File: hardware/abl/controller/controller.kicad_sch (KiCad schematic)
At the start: 38 parts, among them IC2 FXL6408UMX, IC3 VEML6040A3OG, IC4 FXL6408UMX, J1 SFW20S-2STE1LF, J2 Conn_02x05_Odd_Even, J3 Conn_02x05_Odd_Even, J4 PRT-14417, J5 Conn_02x05_Odd_Even, Q2 AO3401A, Q4 AO3401A, U1 INA219AxD, U2 TXB0104RUT

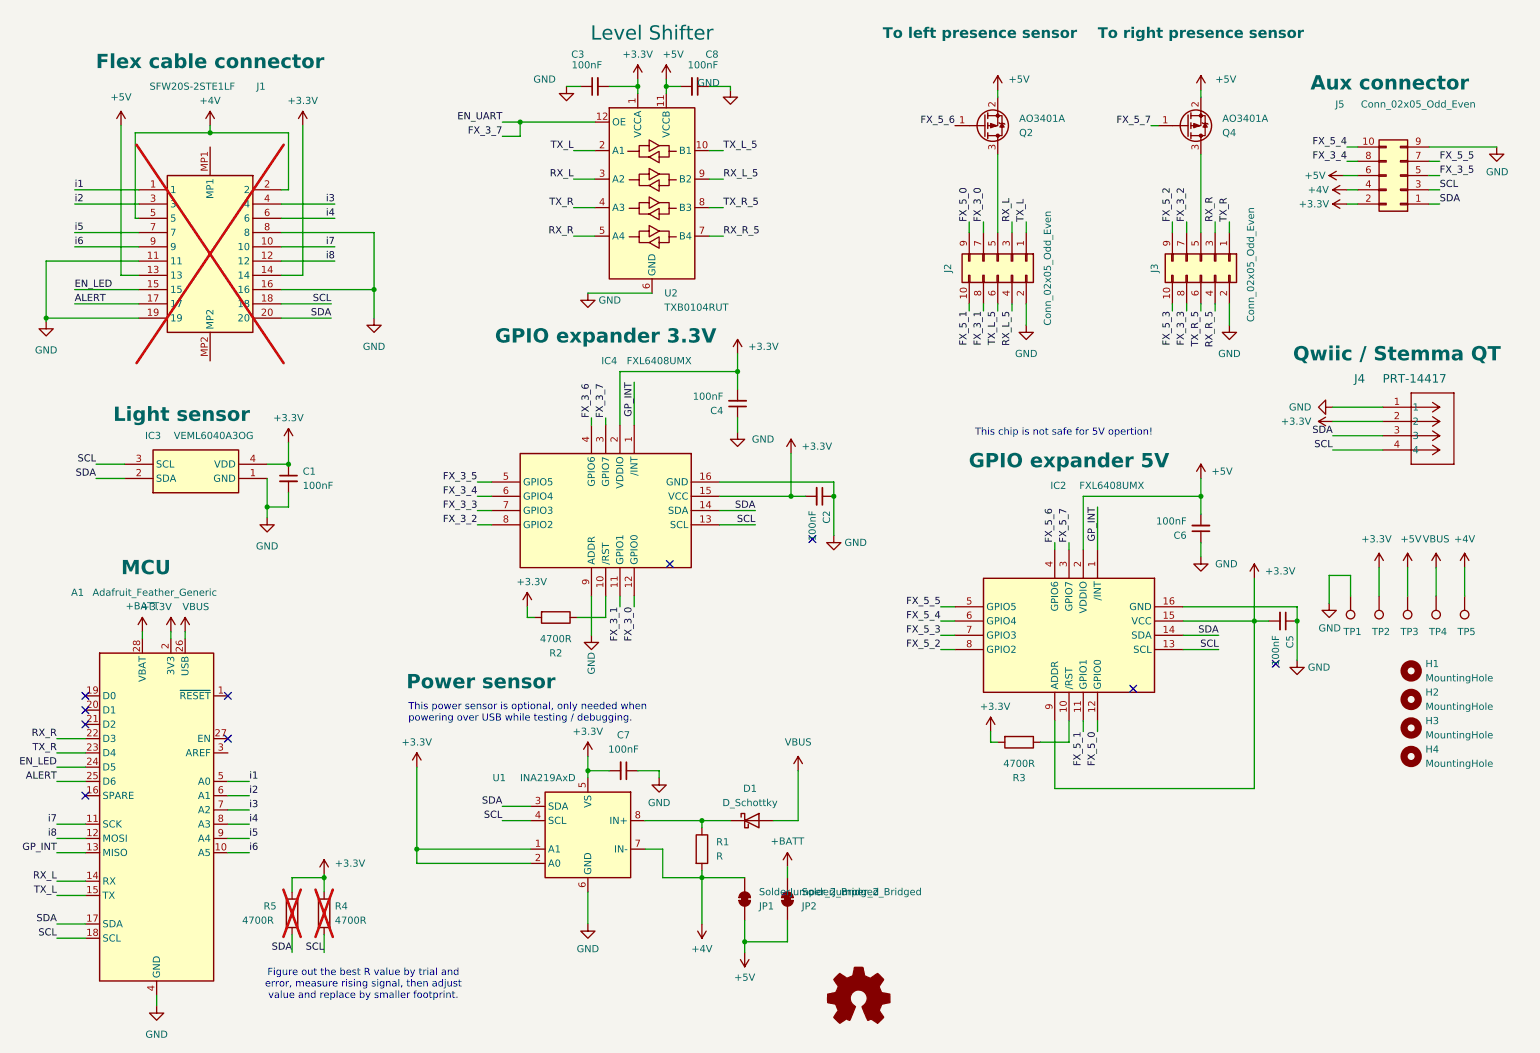
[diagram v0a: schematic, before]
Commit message: Exchanged GPIO Expander for one that supports 5V.
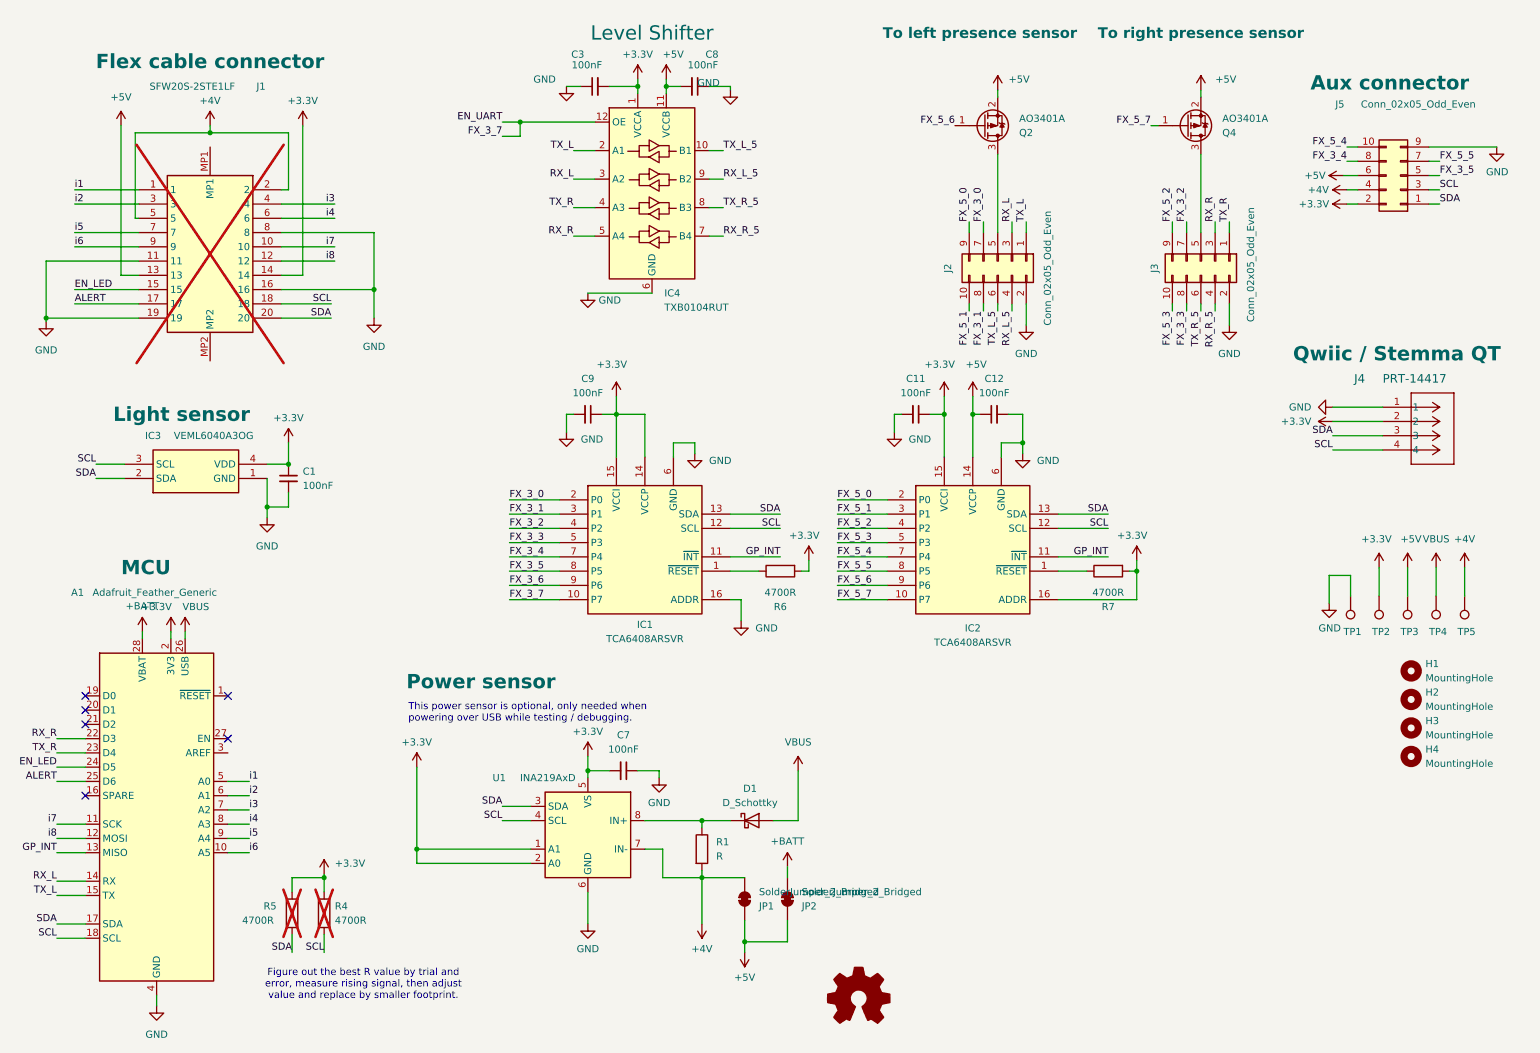
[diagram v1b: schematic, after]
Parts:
- removed C2, C4, C5, C6: 100nF, Capacitor_SMD:C_0402_1005Metric, symbol Device:C_Small
- removed IC2, IC4: FXL6408UMX, QFN40P180X260X55-16N, symbol FXL6408UMX:FXL6408UMX
- removed R2, R3: 4700R, Resistor_SMD:R_0402_1005Metric, symbol Device:R
- added C11, C12, C9: 100nF, Capacitor_SMD:C_0402_1005Metric, symbol Device:C_Small
- added IC1, IC2: TCA6408ARSVR, QFN40P180X260X55-16N, symbol TCA6408ARSVR:TCA6408ARSVR_Own
- added R6, R7: 4700R, Resistor_SMD:R_0402_1005Metric, symbol Device:R
- renumbered U2 to IC4
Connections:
- net +3.3V: now also C11.1, C9.1, IC1.14 (VCCP), IC1.15 (VCCI), IC2.15 (VCCI), IC2.16 (ADDR), R6.2, R7.2
- net +5V: now also C12.1, IC2.14 (VCCP)
- net EN_UART: now also IC1.10 (P7)
- net FX_3_0: now also IC1.2 (P0)
- net FX_3_1: now also IC1.3 (P1)
- net FX_3_2: now also IC1.4 (P2)
- net FX_3_3: now also IC1.5 (P3)
- net FX_3_4: now also IC1.7 (P4)
- net FX_3_5: now also IC1.8 (P5)
- net FX_3_6: now also IC1.9 (P6)
- net FX_5_0: now also IC2.2 (P0)
- net FX_5_1: now also IC2.3 (P1)
- net FX_5_2: now also IC2.4 (P2)
- net FX_5_3: now also IC2.5 (P3)
- net FX_5_4: now also IC2.7 (P4)
- net FX_5_5: now also IC2.8 (P5)
- net FX_5_6: now also IC2.9 (P6)
- net FX_5_7: now also IC2.10 (P7)
- net GND: now also C11.2, C12.2, C9.2, IC1.16 (ADDR), IC1.6 (GND), IC2.6 (GND)
- net GP_INT: now also IC1.11 (~{INT}), IC2.11 (~{INT})
- net SCL: now also IC1.12 (SCL), IC2.12 (SCL)
- net SDA: now also IC1.13 (SDA), IC2.13 (SDA)
- new net: IC1.1 (~{RESET}), R6.1
- new net: IC2.1 (~{RESET}), R7.1
- no-connect marks 10 -> 6

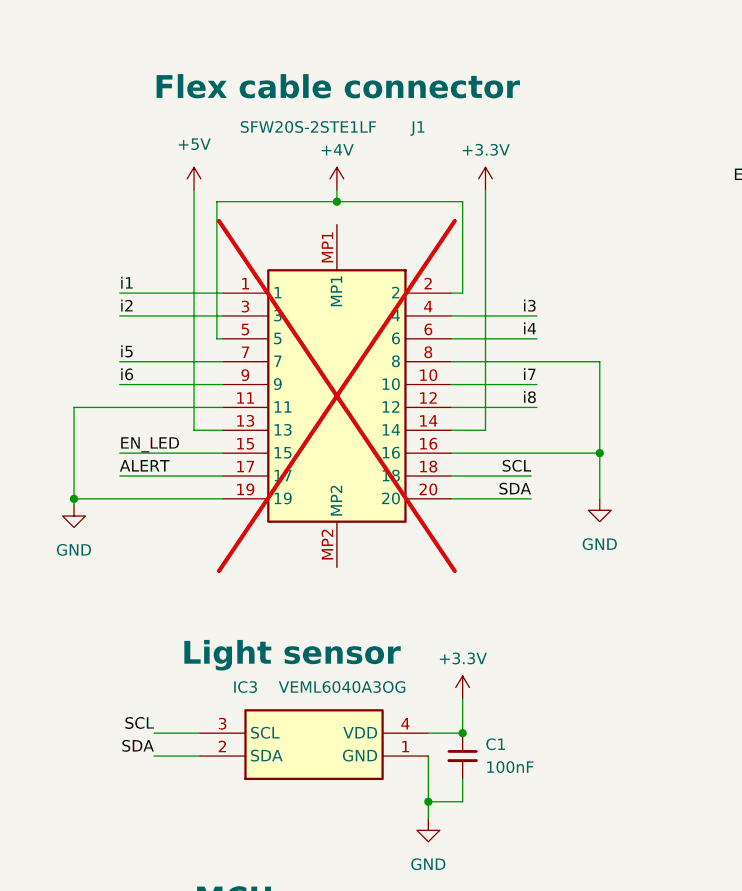
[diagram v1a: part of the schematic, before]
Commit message: Fix orientation of the flex connector.
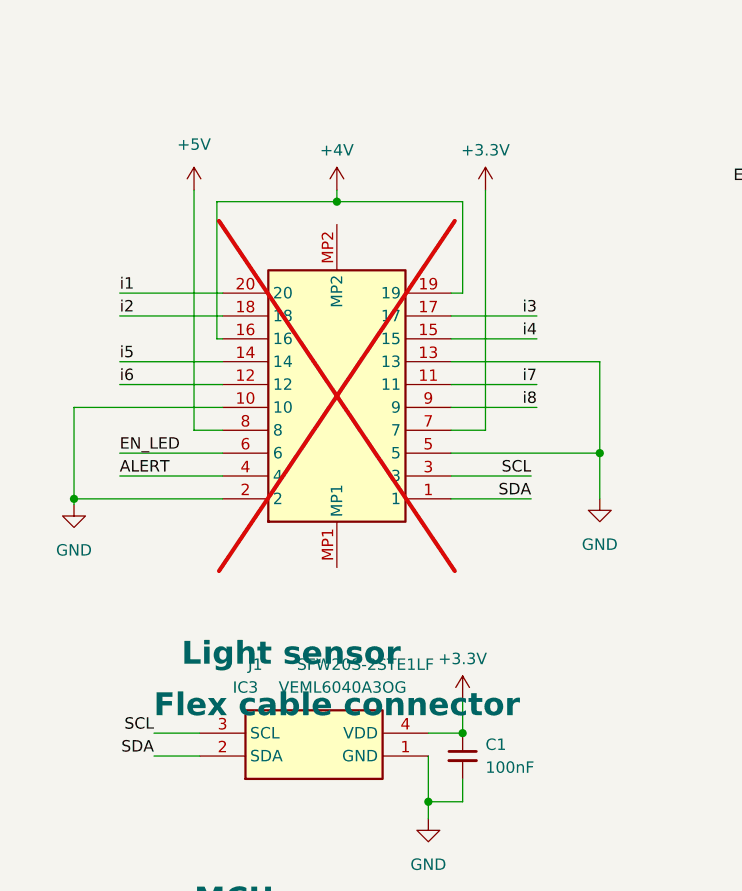
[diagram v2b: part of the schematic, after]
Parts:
- J1: footprint SFW20S2STE1LF -> Own footprints:SFW20S2STE1LF_Own
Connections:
- net +3.3V: now also J1.7; no longer J1.14
- net +4V: now also J1.16, J1.19; no longer J1.2, J1.5
- net +5V: now also J1.8; no longer J1.13
- net ALERT: now also J1.4; no longer J1.17
- net EN_LED: now also J1.6; no longer J1.15
- net GND: now also J1.10, J1.13, J1.2, J1.5; no longer J1.11, J1.16, J1.19, J1.8
- net SCL: now also J1.3; no longer J1.18
- net SDA: now also J1.1; no longer J1.20
- net i1: now also J1.20; no longer J1.1
- net i2: now also J1.18; no longer J1.3
- net i3: now also J1.17; no longer J1.4
- net i4: now also J1.15; no longer J1.6
- net i5: now also J1.14; no longer J1.7
- net i6: now also J1.12; no longer J1.9
- net i7: now also J1.11; no longer J1.10
- net i8: now also J1.9; no longer J1.12
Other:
- moved on the sheet: J1
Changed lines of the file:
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@@
 	(symbol
 		(lib_id "SFW20S-2STE1LF:SFW20S-2STE1LF")
-		(at 50.8 37.465 270)
+		(at 50.8 75.565 90)
 		(unit 1)
 		(exclude_from_sim no)
@@
 		(dnp yes)
 		(property "Reference" "J1"
-			(at 59.055 26.67 90)
+			(at 42.545 86.36 90)
 			(effects
 				(font
@@
 		)
 		(property "Value" "SFW20S-2STE1LF"
-			(at 40.005 26.67 90)
+			(at 61.595 86.36 90)
 			(effects
 				(font
@@
 			)
 		)
-		(property "Footprint" "SFW20S2STE1LF"
-			(at -39.04 71.755 0)
+		(property "Footprint" "Own footprints:SFW20S2STE1LF_Own"
+			(at 140.64 41.275 0)
 			(effects
 				(font
@@
 		)
 		(property "Datasheet" "https://cdn.amphenol-cs.com/media/wysiwyg/files/drawing/10172832.pdf"
-			(at -139.04 71.755 0)
+			(at 240.64 41.275 0)
 			(effects
 				(font
@@
 		)
 		(property "Description" "1.00mm Flex Connector, SFW Straight series, 20 Position, Top Entry Surface Mount, ZIF"
-			(at 50.8 37.465 0)
+			(at 50.8 75.565 0)
 			(effects
 				(font
@@
 		)
 		(property "Height" "5.5"
-			(at -339.04 71.755 0)
+			(at 440.64 41.275 0)
 			(effects
 				(font
@@
 		)
 		(property "Mouser Part Number" ""
-			(at -439.04 71.755 0)
+			(at 540.64 41.275 0)
 			(effects
 				(font
@@
 		)
 		(property "Mouser Price/Stock" ""
-			(at -539.04 71.755 0)
+			(at 640.64 41.275 0)
 			(effects
 				(font
@@
 		)
 		(property "Manufacturer_Name" "Amphenol Communications Solutions"
-			(at -639.04 71.755 0)
+			(at 740.64 41.275 0)
 			(effects
 				(font
@@
 		)
 		(property "Manufacturer_Part_Number" "SFW20S-2STE1LF"
-			(at -739.04 71.755 0)
+			(at 840.64 41.275 0)
 			(effects
 				(font
@@
 		)
 		(property "LCSC Part #" "C5407823"
-			(at 50.8 37.465 0)
+			(at 50.8 75.565 0)
 			(effects
 				(font
@@
 		)
 		(property "Purpose" "Flex cable connector"
-			(at 50.8 22.225 90)
+			(at 50.8 90.805 90)
 			(effects
 				(font

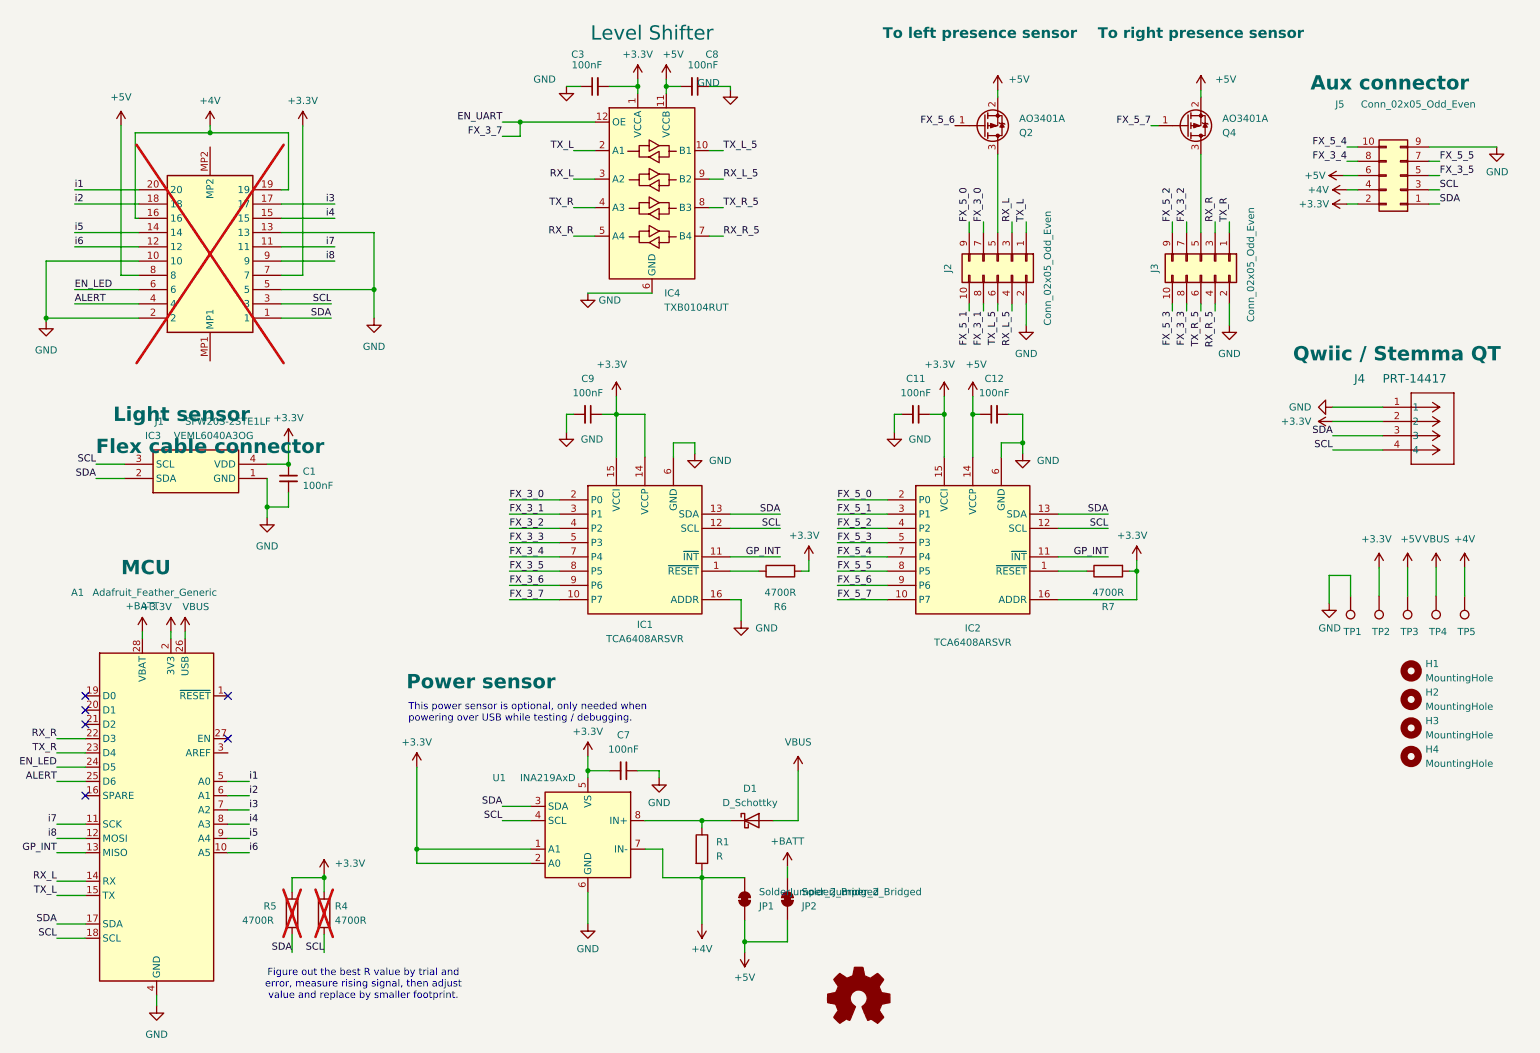
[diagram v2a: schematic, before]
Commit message: Extended with wings to attach presence sensors directly. Removed distinction between VLED and 5V. Much cleanup.
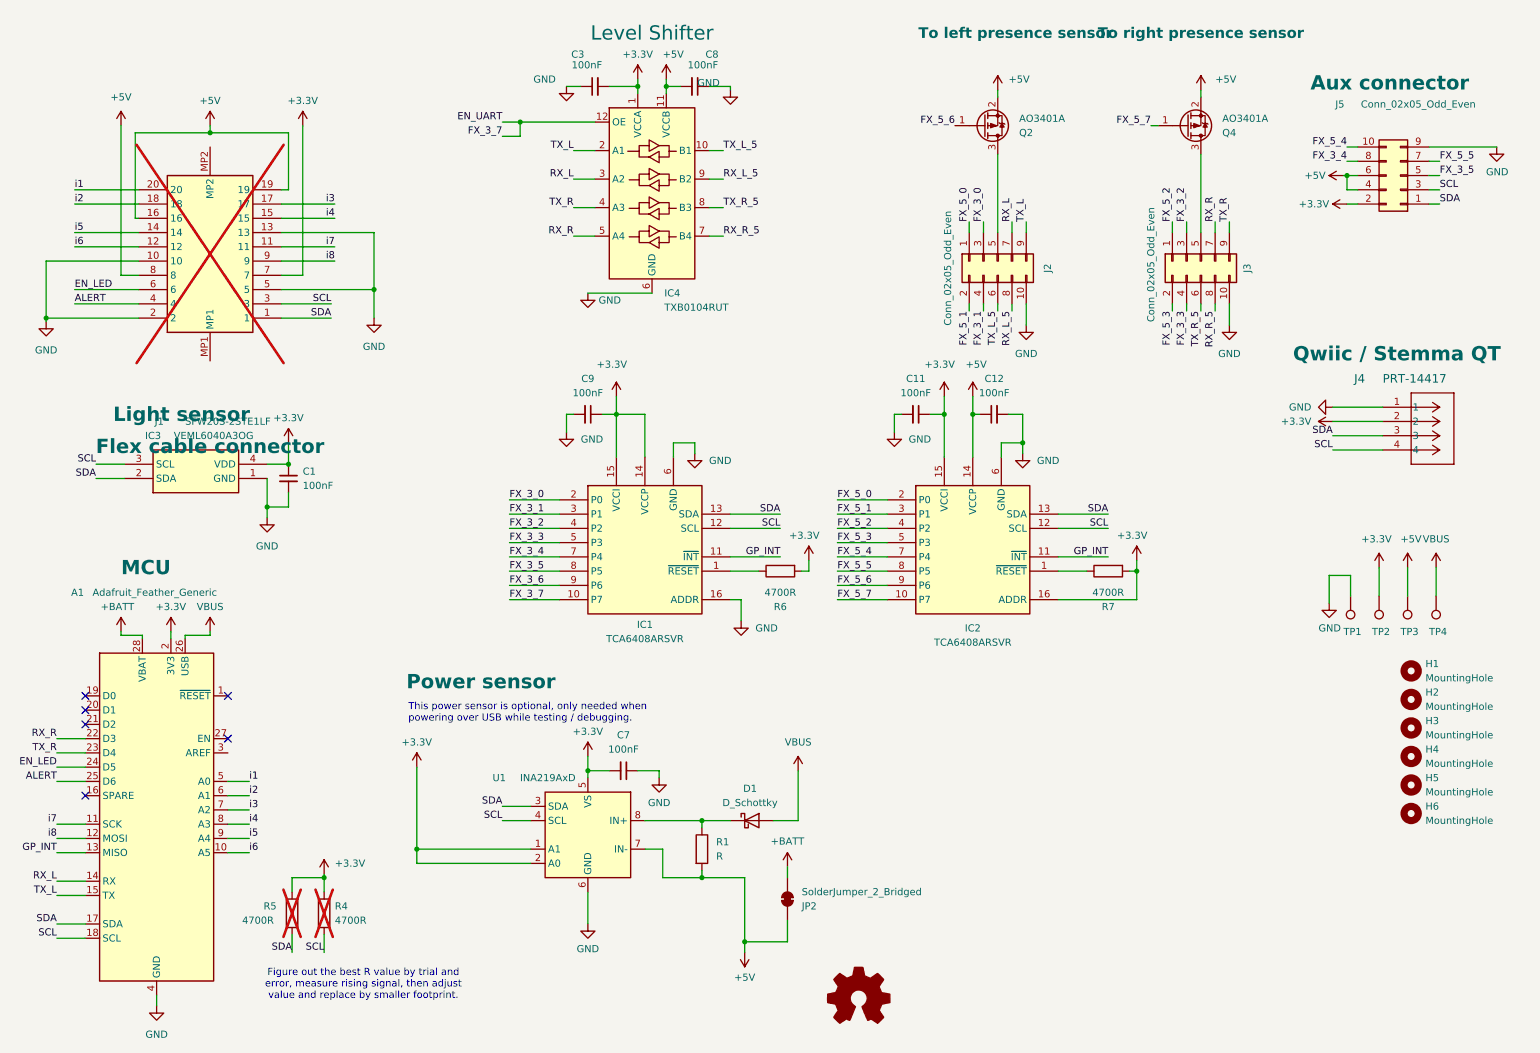
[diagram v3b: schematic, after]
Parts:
- removed JP1: SolderJumper_2_Bridged, Jumper:SolderJumper-2_P1.3mm_Bridged2Bar_RoundedPad1.0x1.5mm, symbol Jumper:SolderJumper_2_Bridged
- removed TP5: TestPoint, TestPoint:TestPoint_THTPad_D1.5mm_Drill0.7mm, symbol Connector:TestPoint
- added H5, H6: MountingHole, MountingHole:MountingHole_3.2mm_M3_DIN965, symbol Mechanical:MountingHole
- J2, J3: footprint Connector_IDC:IDC-Header_2x05_P2.54mm_Vertical -> Own footprints:Dual Row Inverted Thru Board Card Edge Connector 02x05 Kyocera AVX 009159010603906
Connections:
- net  FX_5_1 is gone; now on net GND: J2.10 (Pin_10)
- net +4V is gone; now on net +5V: J1.16, J1.19, J5.4 (Pin_4), R1.2, U1.7 (IN-)
- net FX_3_0: now also J2.3 (Pin_3); no longer J2.7 (Pin_7)
- net FX_3_1: now also J2.4 (Pin_4); no longer J2.8 (Pin_8)
- net FX_3_2: now also J3.3 (Pin_3); no longer J3.7 (Pin_7)
- net FX_3_3: now also J3.4 (Pin_4); no longer J3.8 (Pin_8)
- net FX_5_0: now also J2.1 (Pin_1); no longer J2.9 (Pin_9)
- net FX_5_1: now also J2.2 (Pin_2)
- net FX_5_2: now also J3.1 (Pin_1); no longer J3.9 (Pin_9)
- net FX_5_3: now also J3.2 (Pin_2); no longer J3.10 (Pin_10)
- net GND: now also J3.10 (Pin_10); no longer J2.2 (Pin_2), J3.2 (Pin_2)
- net RX_L: now also J2.7 (Pin_7); no longer J2.3 (Pin_3)
- net RX_L_5: now also J2.8 (Pin_8); no longer J2.4 (Pin_4)
- net RX_R: now also J3.7 (Pin_7); no longer J3.3 (Pin_3)
- net RX_R_5: now also J3.8 (Pin_8); no longer J3.4 (Pin_4)
- net TX_L: now also J2.9 (Pin_9); no longer J2.1 (Pin_1)
- net TX_R: now also J3.9 (Pin_9); no longer J3.1 (Pin_1)
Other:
- moved on the sheet: J2, J3

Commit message: Many, many minor updates to the big PCBs, and a few simple helper PCBs.
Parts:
- added J6, J7: Conn_01x10_Pin, Connector_PinHeader_2.54mm:PinHeader_1x10_P2.54mm_Vertical, symbol Connector:Conn_01x10_Pin
- A1, H1, H2, H3, H4, H5, H6, J2, J3, J5, JP2, TP1, TP2, TP3, TP4: now not fitted
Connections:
- net GND: now also J6.1 (Pin_1), J6.10 (Pin_10), J6.2 (Pin_2), J6.3 (Pin_3), J6.4 (Pin_4), J6.5 (Pin_5), J6.6 (Pin_6), J6.7 (Pin_7), J6.8 (Pin_8), J6.9 (Pin_9), J7.1 (Pin_1), J7.10 (Pin_10), J7.2 (Pin_2), J7.3 (Pin_3), J7.4 (Pin_4), J7.5 (Pin_5), J7.6 (Pin_6), J7.7 (Pin_7), J7.8 (Pin_8), J7.9 (Pin_9)
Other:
- moved on the sheet: C11, C12, C7, C9, D1, IC1, IC2, Q2, Q4, R1, R4, R5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
